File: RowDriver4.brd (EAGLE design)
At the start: 100 x 80 mm, 98 parts, among them Q1 DPBT8105, Q10 DPBT8105, Q11 DPBT8105, Q12 DPBT8105, Q13 DPBT8105, Q14 DPBT8105, Q15 DPBT8105, Q16 DPBT8105, Q2 DPBT8105, Q3 DPBT8105, Q4 DPBT8105, Q5 DPBT8105, Q6 DPBT8105, Q7 DPBT8105, Q8 DPBT8105, Q9 DPBT8105

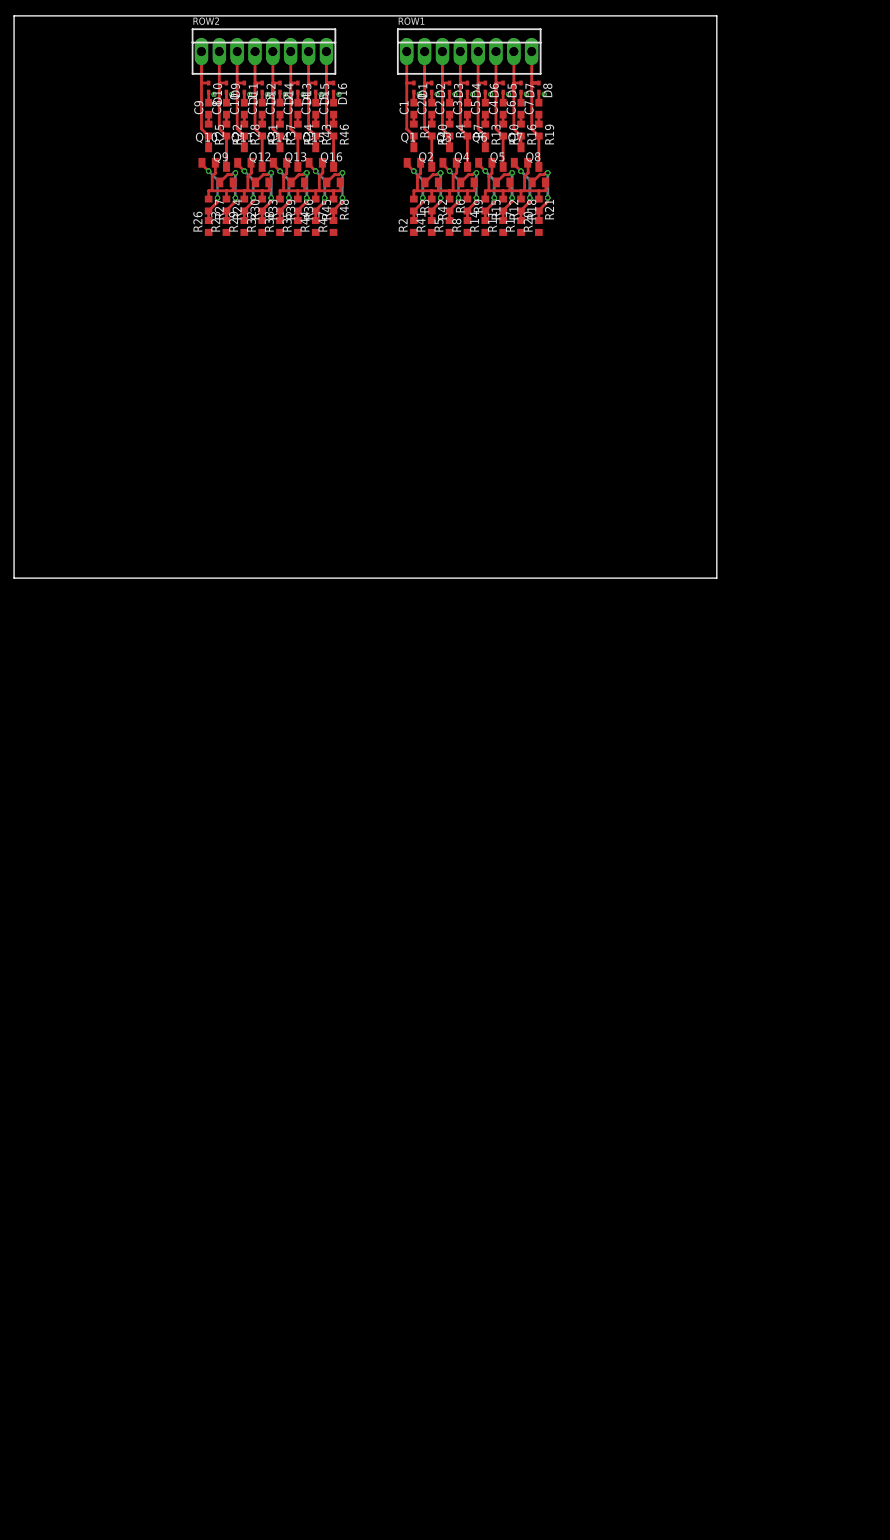
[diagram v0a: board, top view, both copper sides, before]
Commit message: Iterated through a few possible board floorplans.  Routing will be incredibly tight, but I thought of a few possibilities that ease those concerns.
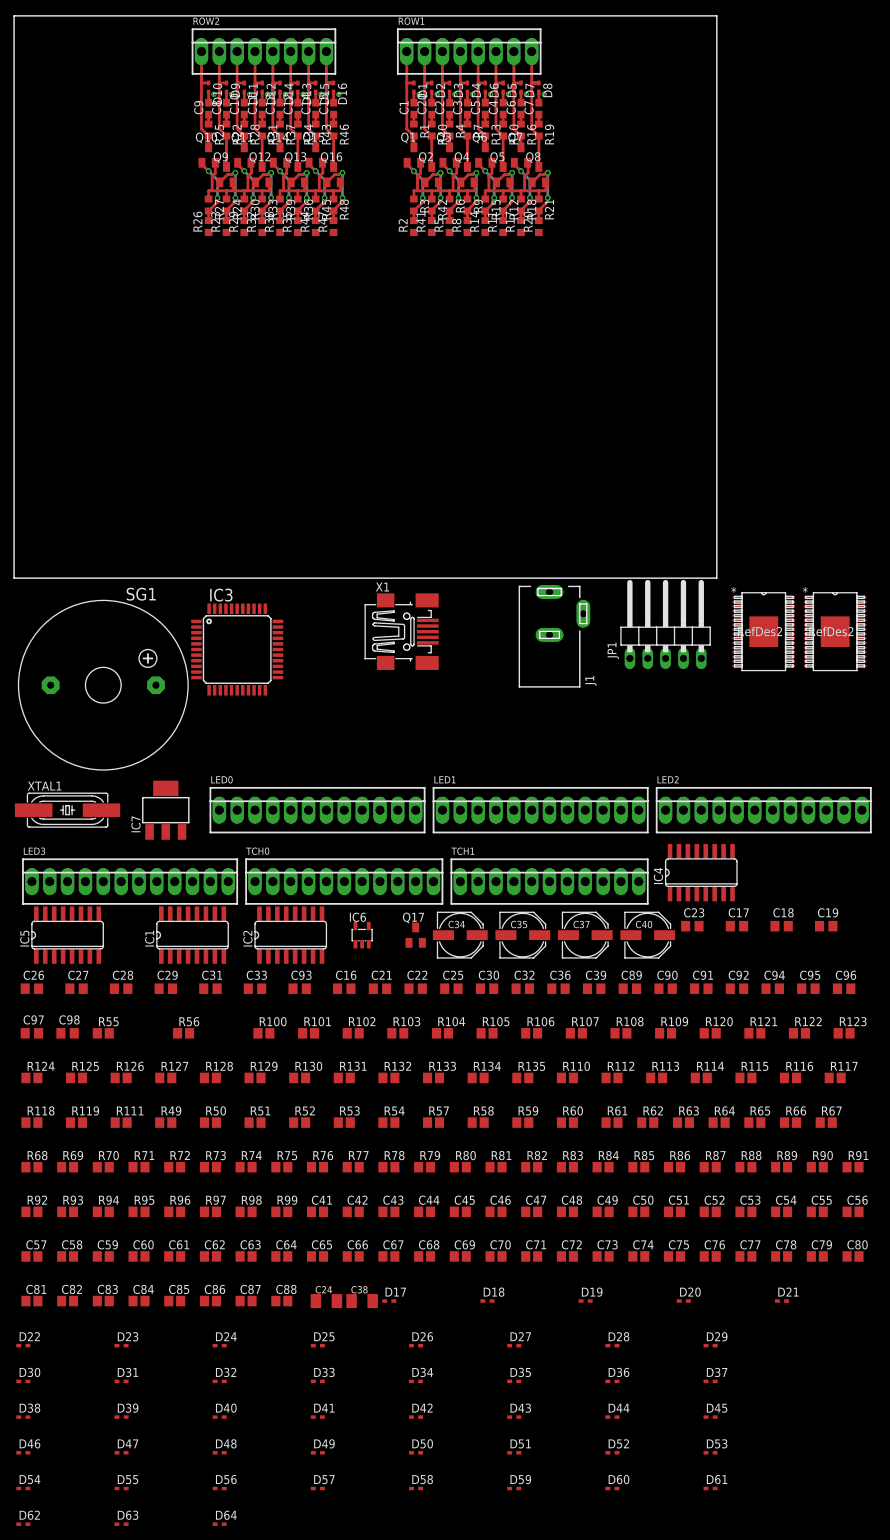
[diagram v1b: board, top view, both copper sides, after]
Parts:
- added C16, C21, C22, C89, C90, C91, C92, C94, C95, C96, C97, C98: NC, rcl:C0805
- added C17, C18, C19, C26, C27, C28, C29, C31, C33, C93: 0.1uF, rcl:C0805
- added C23: 470pF, rcl:C0805
- added C24, C38: 10uF, rcl:C1206K
- added C25, C30, C32, C36, C39: 1uF, rcl:C0805
- added C34, C35, C37, C40: 100uF, resistor:PANASONIC_D
- added C41, C42, C43, C44, C45, C46, C47, C48, C49, C50, C51, C52, C53, C54, C55, C56, C57, C58, C59, C60, C61, C62, C63, C64, C65, C66, C67, C68, C69, C70, C71, C72, C73, C74, C75, C76, C77, C78, C79, C80, C81, C82, C83, C84, C85, C86, C87, C88: 1n, resistor:C0805
- added D17, D18, D19, D20, D21, D22, D23, D24, D25, D26, D27, D28, D29, D30, D31, D32, D33, D34, D35, D36, D37, D38, D39, D40, D41, D42, D43, D44, D45, D46, D47, D48, D49, D50, D51, D52, D53, D54, D55, D56, D57, D58, D59, D60, D61, D62, D63, D64: RB521S30T1G, diode:SOD523
- added IC1, IC2: 74HCT138D, Parts:SO16
- added IC3: PIC24FJ32GB004, Parts:TQFP44
- added IC4, IC5: SN74LV4052AD, Parts:SO16
- added IC6: TC1015, Parts:SOT23-5L
- added IC7: NCP1117, Parts:SOT223
- added J1: PWR, con-jack:DCJ0303
- added JP1: DEBUG, pinhead:1X05/90
- added LED0, LED1, LED2, LED3: (no value), Parts:OSTVN12
- added Q17: NC, transistor:SOT23-EBC
- added R100, R101, R102, R103, R104, R105, R106, R107, R108, R109, R110, R111, R112, R113, R114, R115, R116, R117, R118, R119, R120, R121, R122, R123, R124, R125, R126, R127, R128, R129, R130, R131, R132, R133, R134, R135, R88, R89, R90, R91, R92, R93, R94, R95, R96, R97, R98, R99: 300, resistor:R0805
- added R49, R50, R51, R52, R53, R54, R57, R58, R59, R60: 4.7k, resistor:R0805
- added R55, R56: 1.37k 0.5%, resistor:R0805
- added R61, R62, R63, R64, R65, R66, R67, R68, R69, R70, R71, R72, R73, R74, R75, R76, R77, R78, R79, R80, R81, R82, R83: 390, resistor:R0805
- added R84: 0, resistor:R0805
- added R85, R86, R87: NC, resistor:R0805
- added SG1: NC, buzzer:F/CM04P
- added TCH0, TCH1: (no value), Parts:OSTVN11
- added U$1, U$2: TLC5952, Parts:HTSSOP-32POWERPAD
- added X1: MINI-USB-32005-201, Parts:32005-201
- added XTAL1: NC, crystal:HC49UP
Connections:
- new net +3V3: C17.1, C18.1, C19.1, C24.1, C26.1, C27.1, C30.1, C31.1, C32.1, C33.1, C89.1, C90.1, C91.1, C93.1, C94.1, C95.1, C98.1, IC3.10, IC3.17, IC3.28, IC3.40, IC4.16, IC5.16, IC6.5, JP1.2, R60.2, R85.2, U$1.31, U$2.31
- new net AMSEL0: IC3.44, IC4.10, IC5.10
- new net AMSEL1: IC3.1, IC4.9, IC5.9
- new net B0: D19.A, LED0.3, R90.2, U$1.7
- new net B1: D22.A, LED0.6, R93.2, U$1.10
- new net B10: D49.A, LED2.9, R120.2, U$2.13
- new net B11: D52.A, LED2.12, R123.2, U$2.16
- new net B12: D55.A, LED3.3, R126.2, U$2.19
- new net B13: D58.A, LED3.6, R129.2, U$2.22
- new net B14: D61.A, LED3.9, R132.2, U$2.25
- new net B15: D64.A, LED3.12, R135.2, U$2.28
- new net B2: D25.A, LED0.9, R96.2, U$1.13
- new net B3: D28.A, LED0.12, R99.2, U$1.16
- new net B4: D31.A, LED1.3, R102.2, U$1.19
- new net B5: D34.A, LED1.6, R105.2, U$1.22
- new net B6: D37.A, LED1.9, R108.2, U$1.25
- new net B7: D40.A, LED1.12, R111.2, U$1.28
- new net B8: D43.A, LED2.3, R114.2, U$2.7
- new net B9: D46.A, LED2.6, R117.2, U$2.10
- new net C0_LAT: IC3.33, U$1.4
- new net C0_SCLK: IC3.37, U$1.3
- new net C0_SIN: IC3.38, U$1.2
- new net C0_SOUT: IC3.43, U$1.30
- new net C1_LAT: IC3.2, U$2.4
- new net C1_SCLK: IC3.3, U$2.3
- new net C1_SIN: IC3.4, U$2.2
- new net C1_SOUT: IC3.5, U$2.30
- new net CAIREF: R55.2, U$1.32
- new net CAIREF1: R56.2, U$2.32
- new net C_BLANK: IC3.41, U$1.29, U$2.29
- new net D+: IC3.8, X1.3
- new net D-: IC3.9, X1.2
- new net DISVREG: IC3.6, R59.2
- new net G0: D18.A, LED0.2, R89.2, U$1.6
- new net G1: D21.A, LED0.5, R92.2, U$1.9
- new net G10: D48.A, LED2.8, R119.2, U$2.12
- new net G11: D51.A, LED2.11, R122.2, U$2.15
- new net G12: D54.A, LED3.2, R125.2, U$2.18
- new net G13: D57.A, LED3.5, R128.2, U$2.21
- new net G14: D60.A, LED3.8, R131.2, U$2.24
- new net G15: D63.A, LED3.11, R134.2, U$2.27
- new net G2: D24.A, LED0.8, R95.2, U$1.12
- new net G3: D27.A, LED0.11, R98.2, U$1.15
- new net G4: D30.A, LED1.2, R101.2, U$1.18
- new net G5: D33.A, LED1.5, R104.2, U$1.21
- new net G6: D36.A, LED1.8, R107.2, U$1.24
- new net G7: D39.A, LED1.11, R110.2, U$1.27
- new net G8: D42.A, LED2.2, R113.2, U$2.6
- new net G9: D45.A, LED2.5, R116.2, U$2.9
- new net MCLR_: IC3.18, JP1.1, R61.1
- new net N$100: C52.1, R99.1
- new net N$101: C53.1, R100.1
- new net N$102: C54.1, R101.1
- new net N$103: C55.1, R102.1
- new net N$104: C56.1, R103.1
- new net N$105: C57.1, R104.1
- new net N$106: C58.1, R105.1
- new net N$107: C59.1, R106.1
- new net N$108: C60.1, R107.1
- new net N$109: C61.1, R108.1
- new net N$110: C62.1, R109.1
- new net N$111: C63.1, R110.1
- new net N$112: C64.1, R111.1
- new net N$114: C65.1, R112.1
- new net N$116: C66.1, R113.1
- new net N$118: C67.1, R114.1
- new net N$120: C68.1, R115.1
- new net N$122: C69.1, R116.1
- new net N$124: C70.1, R117.1
- new net N$126: C71.1, R118.1
- new net N$128: C72.1, R119.1
- new net N$130: C73.1, R120.1
- new net N$132: C74.1, R121.1
- new net N$134: C75.1, R122.1
- new net N$136: C76.1, R123.1
- new net N$138: C77.1, R124.1
- new net N$140: C78.1, R125.1
- new net N$142: C79.1, R126.1
- new net N$144: C80.1, R127.1
- new net N$146: C81.1, R128.1
- new net N$148: C82.1, R129.1
- new net N$150: C83.1, R130.1
- new net N$152: C84.1, R131.1
- new net N$154: C85.1, R132.1
- new net N$156: C86.1, R133.1
- new net N$158: C87.1, R134.1
- new net N$160: C88.1, R135.1
- new net N$41: IC1.4, IC1.5, R50.2
- new net N$42: IC4.6, R51.2
- new net N$43: IC2.4, IC2.5, R53.2
- new net N$44: IC5.6, R54.2
- new net N$45: IC3.42, R58.2
- new net N$46: C16.1, R60.1, R61.2
- new net N$47: R62.2, TCH0.1
- new net N$48: R63.2, TCH0.2
- new net N$65: R64.2, TCH0.3
- new net N$66: R65.2, TCH0.4
- new net N$67: R66.2, TCH0.5
- new net N$68: R67.2, TCH0.6
- new net N$69: R68.2, TCH0.7
- new net N$70: R69.2, TCH0.8
- new net N$71: R70.2, TCH0.9
- new net N$72: R71.2, TCH0.10
- new net N$73: R72.2, TCH0.11
- new net N$74: R74.2, TCH1.2
- new net N$75: R76.2, TCH1.4
- new net N$76: R78.2, TCH1.6
- new net N$77: R80.2, TCH1.8
- new net N$78: R82.2, TCH1.10
- new net N$79: R73.2, TCH1.1
- new net N$80: R75.2, TCH1.3
- new net N$81: R77.2, TCH1.5
- new net N$82: R79.2, TCH1.7
- new net N$83: R81.2, TCH1.9
- new net N$84: R83.2, TCH1.11
- new net N$85: C23.1, IC6.4
- new net N$86: R85.1, R86.2
- new net N$87: Q17.B, R87.2
- new net N$88: Q17.C, SG1.-
- new net N$89: C41.1, R88.1
- new net N$90: C42.1, R89.1
- new net N$91: C43.1, R90.1
- new net N$92: C44.1, R91.1
- new net N$93: C45.1, R92.1
- new net N$94: C46.1, R93.1
- new net N$95: C47.1, R94.1
- new net N$96: C48.1, R95.1
- new net N$97: C49.1, R96.1
- new net N$98: C50.1, R97.1
- new net N$99: C51.1, R98.1
- new net OSCI: C22.1, IC3.30, XTAL1.1
- new net OSCO: C21.1, IC3.31, XTAL1.2
- new net PGEC: IC3.22, JP1.5
- new net PGED: IC3.21, JP1.4
- new net R0: D17.A, LED0.1, R88.2, U$1.5
- new net R1: D20.A, LED0.4, R91.2, U$1.8
- new net R10: D47.A, LED2.7, R118.2, U$2.11
- new net R11: D50.A, LED2.10, R121.2, U$2.14
- new net R12: D53.A, LED3.1, R124.2, U$2.17
- new net R13: D56.A, LED3.4, R127.2, U$2.20
- new net R14: D59.A, LED3.7, R130.2, U$2.23
- new net R15: D62.A, LED3.10, R133.2, U$2.26
- new net R2: D23.A, LED0.7, R94.2, U$1.11
- new net R3: D26.A, LED0.10, R97.2, U$1.14
- new net R4: D29.A, LED1.1, R100.2, U$1.17
- new net R5: D32.A, LED1.4, R103.2, U$1.20
- new net R6: D35.A, LED1.7, R106.2, U$1.23
- new net R7: D38.A, LED1.10, R109.2, U$1.26
- new net R8: D41.A, LED2.1, R112.2, U$2.5
- new net R9: D44.A, LED2.4, R115.2, U$2.8
- new net RAEN: IC1.6, IC3.12, R49.2
- new net RBEN: IC2.6, IC3.34, R52.2
- new net RSEL0: IC1.1, IC2.1, IC3.13
- new net RSEL1: IC1.2, IC2.2, IC3.32
- new net RSEL2: IC1.3, IC2.3, IC3.35
- new net TMUX0: IC3.11, IC4.3
- new net TMUX1: IC3.14, IC4.13
- new net TMUX2: IC3.24, IC5.3
- new net TMUX3: IC3.25, IC5.13
- new net TOUCH0: IC4.1, R62.1
- new net TOUCH1: IC4.5, R63.1
- new net TOUCH10: IC3.23, R72.1
- new net TOUCH11: IC5.1, R73.1
- new net TOUCH12: IC5.5, R74.1
- new net TOUCH13: IC5.2, R75.1
- new net TOUCH14: IC5.4, R76.1
- new net TOUCH15: IC5.12, R77.1
- new net TOUCH16: IC5.14, R78.1
- new net TOUCH17: IC5.15, R79.1
- new net TOUCH18: IC5.11, R80.1
- new net TOUCH19: IC3.26, R81.1
- new net TOUCH2: IC4.2, R64.1
- new net TOUCH20: IC3.27, R82.1
- new net TOUCH21: IC3.36, R83.1
- new net TOUCH3: IC4.4, R65.1
- new net TOUCH4: IC4.12, R66.1
- new net TOUCH5: IC4.14, R67.1
- new net TOUCH6: IC4.15, R68.1
- new net TOUCH7: IC4.11, R69.1
- new net TOUCH8: IC3.15, R70.1
- new net TOUCH9: IC3.20, R71.1
- new net V+: C35.+, IC7.3, J1.1, R84.1
- new net VBUS: R57.2, R58.1, X1.1
- new net VDDCORE: C38.1, C92.1, IC3.7
- new net VREF+: IC3.19, R87.1
- net +5V: now also C25.1, C28.1, C29.1, C34.+, C36.1, C37.+, C39.1, C40.+, C96.1, C97.1, D17.C, D18.C, D19.C, D20.C, D21.C, D22.C, D23.C, D24.C, D25.C, D26.C, D27.C, D28.C, D29.C, D30.C, D31.C, D32.C, D33.C, D34.C, D35.C, D36.C, D37.C, D38.C, D39.C, D40.C, D41.C, D42.C, D43.C, D44.C, D45.C, D46.C, D47.C, D48.C, D49.C, D50.C, D51.C, D52.C, D53.C, D54.C, D55.C, D56.C, D57.C, D58.C, D59.C, D60.C, D61.C, D62.C, D63.C, D64.C, IC1.16, IC2.16, IC6.1, IC6.3, IC7.2, R84.2, SG1.+
- net GND: now also C16.2, C17.2, C18.2, C19.2, C21.2, C22.2, C23.2, C24.2, C25.2, C26.2, C27.2, C28.2, C29.2, C30.2, C31.2, C32.2, C33.2, C34.-, C35.-, C36.2, C37.-, C38.2, C39.2, C40.-, C41.2, C42.2, C43.2, C44.2, C45.2, C46.2, C47.2, C48.2, C49.2, C50.2, C51.2, C52.2, C53.2, C54.2, C55.2, C56.2, C57.2, C58.2, C59.2, C60.2, C61.2, C62.2, C63.2, C64.2, C65.2, C66.2, C67.2, C68.2, C69.2, C70.2, C71.2, C72.2, C73.2, C74.2, C75.2, C76.2, C77.2, C78.2, C79.2, C80.2, C81.2, C82.2, C83.2, C84.2, C85.2, C86.2, C87.2, C88.2, C89.2, C90.2, C91.2, C92.2, C93.2, C94.2, C95.2, C96.2, C97.2, C98.2, IC1.8, IC2.8, IC3.16, IC3.29, IC3.39, IC4.7, IC4.8, IC5.7, IC5.8, IC6.2, IC7.1, IC7.4, J1.2, J1.3, JP1.3, Q17.E, R49.1, R50.1, R51.1, R52.1, R53.1, R54.1, R55.1, R56.1, R57.1, R59.1, R86.1, U$1.1, U$1.33, U$2.1, U$2.33, X1.5
- net ROW0EN_: now also IC1.15
- net ROW10EN_: now also IC2.13
- net ROW11EN_: now also IC2.12
- net ROW12EN_: now also IC2.11
- net ROW13EN_: now also IC2.10
- net ROW14EN_: now also IC2.9
- net ROW15EN_: now also IC2.7
- net ROW1EN_: now also IC1.14
- net ROW2EN_: now also IC1.13
- net ROW3EN_: now also IC1.12
- net ROW4EN_: now also IC1.11
- net ROW5EN_: now also IC1.10
- net ROW6EN_: now also IC1.9
- net ROW7EN_: now also IC1.7
- net ROW8EN_: now also IC2.15
- net ROW9EN_: now also IC2.14
